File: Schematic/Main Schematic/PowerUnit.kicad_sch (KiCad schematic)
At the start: 19 parts

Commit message: Update
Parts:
- added TP13: TestPoint, symbol Connector:TestPoint
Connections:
- net at C?.1, J?.1 (Pin_1), J?.2 (Pin_2)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: now also TP13.1
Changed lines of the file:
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@@
   (junction (at 54.6608 57.2008) (diameter 0) (color 0 0 0 0)
+  )
+  (junction (at 56.4896 148.59) (diameter 0) (color 0 0 0 0)
   )
   (junction (at 142.24 45.72) (diameter 0) (color 0 0 0 0)
@@
     (stroke (width 0) (type default))
   )
-  (wire (pts (xy 53.086 148.59) (xy 63.5 148.59))
+  (wire (pts (xy 53.086 148.59) (xy 56.4896 148.59))
     (stroke (width 0) (type default))
   )
@@
   )
   (wire (pts (xy 99.06 77.47) (xy 99.06 88.9))
+    (stroke (width 0) (type default))
+  )
+  (wire (pts (xy 56.4896 148.59) (xy 63.5 148.59))
     (stroke (width 0) (type default))
   )
@@
   (hierarchical_label "3.3V" (shape input) (at 102.87 148.59 0) (fields_autoplaced)
     (effects (font (size 1.27 1.27)) (justify left))
-  )
-  (netclass_flag "" (length 3) (shape round) (at 57.15 148.59 0) (fields_autoplaced)
-    (effects (font (size 1.27 1.27)) (justify left bottom))
-    (property "Netclass" "" (at 57.8485 145.59 0)
-      (effects (font (size 1.27 1.27) italic) (justify left))
-    )
   )
   (symbol (lib_id "pspice:CAP") (at 53.086 156.21 0) (unit 1)
@@
         )
       )
+    )
+  )
+  (symbol (lib_id "Connector:TestPoint") (at 56.4896 148.59 0) (unit 1)
+    (in_bom yes) (on_board yes) (dnp no) (fields_autoplaced)
+    (property "Reference" "TP13" (at 58.42 144.653 0)
+      (effects (font (size 1.27 1.27)) (justify left))
+    )
+    (property "Value" "TestPoint" (at 58.42 147.193 0)
+      (effects (font (size 1.27 1.27)) (justify left))
+    )
+    (property "Footprint" "" (at 61.5696 148.59 0)
+      (effects (font (size 1.27 1.27)) hide)
+    )
+    (property "Datasheet" "~" (at 61.5696 148.59 0)
+      (effects (font (size 1.27 1.27)) hide)
+    )
+    (pin "1")
+    (instances
+      (project "Main Schematic"
+        (path "/81c41bad-bb43-41af-b405-18d135a809b1/297def35-fe1a-4185-9e34-6248c2c818f7"
+          (reference "TP13") (unit 1)
+        )
+      )

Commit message: assigned footprints for most of the components
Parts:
- C?: footprint (none) -> 10uFcapa:CAPC1608X100N
- R2: footprint (none) -> 1K_R:RESC1005X40N
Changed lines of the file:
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@@
       (effects (font (size 1.27 1.27)) (justify left))
     )
-    (property "Footprint" "" (at 110.1852 55.88 0)
+    (property "Footprint" "10uFcapa:CAPC1608X100N" (at 110.1852 55.88 0)
       (effects (font (size 1.27 1.27)) hide)
     )
@@
       (effects (font (size 1.27 1.27)) (justify left))
     )
-    (property "Footprint" "" (at 97.282 73.66 90)
+    (property "Footprint" "1K_R:RESC1005X40N" (at 97.282 73.66 90)
       (effects (font (size 1.27 1.27)) hide)
     )

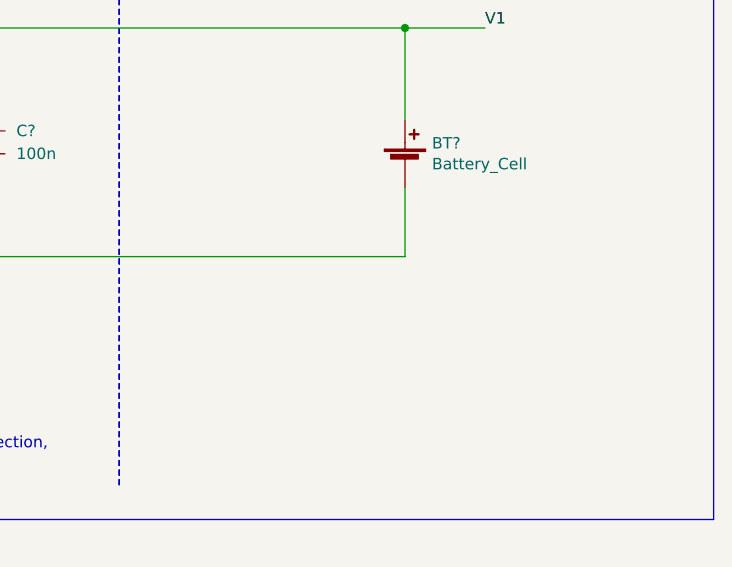
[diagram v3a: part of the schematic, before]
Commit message: Updated the footprints and the PCB
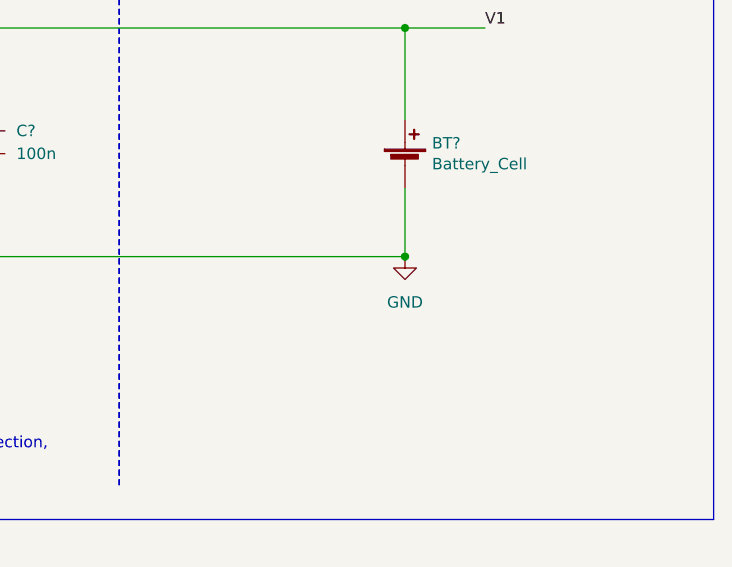
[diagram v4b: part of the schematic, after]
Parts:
- BT?: footprint (none) -> Battery:BatteryHolder_Keystone_3034_1x20mm
- C? (x3): footprint 10uFcapa:CAPC1608X100N -> Capacitor_SMD:C_0402_1005Metric
- C?: footprint (none) -> Capacitor_SMD:C_0201_0603Metric
- C?: footprint 10uFcapa:CAPC1608X100N -> Capacitor_SMD:C_1206_3216Metric_Pad1.33x1.80mm_HandSolder
- D1: footprint (none) -> Capacitor_SMD:C_1206_3216Metric
- J?: footprint (none) -> Connector_USB:USB_Micro-B_GCT_USB3076-30-A
- R3: footprint (none) -> Resistor_SMD:R_1206_3216Metric
- TP13: footprint (none) -> TestPoint:TestPoint_Pad_1.0x1.0mm
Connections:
- net GND: now also BT?.2 (-), C?.2, IC?.6 (GND), Q?.6 (S2_1), Q?.7 (S2_2)
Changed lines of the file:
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@@
   (junction (at 46.355 148.59) (diameter 0) (color 0 0 0 0)
+  )
+  (junction (at 251.46 83.82) (diameter 0) (color 0 0 0 0)
   )
   (junction (at 95.25 57.15) (diameter 0) (color 0 0 0 0)
@@
       (effects (font (size 1.27 1.27)) (justify left))
     )
-    (property "Footprint" "10uFcapa:CAPC1608X100N" (at 53.086 156.21 0)
+    (property "Footprint" "Capacitor_SMD:C_0402_1005Metric" (at 53.086 156.21 0)
       (effects (font (size 1.27 1.27)) hide)
     )
@@
       (effects (font (size 1.27 1.27)))
     )
-    (property "Footprint" "" (at 35.6108 74.93 0)
+    (property "Footprint" "Connector_USB:USB_Micro-B_GCT_USB3076-30-A" (at 35.6108 74.93 0)
       (effects (font (size 1.27 1.27)) hide)
     )
@@
       (effects (font (size 1.27 1.27)) (justify right))
     )
-    (property "Footprint" "" (at 99.06 92.71 0)
+    (property "Footprint" "Capacitor_SMD:C_1206_3216Metric" (at 99.06 92.71 0)
       (effects (font (size 1.27 1.27)) hide)
     )
@@
       (effects (font (size 1.27 1.27)) (justify left))
     )
-    (property "Footprint" "10uFcapa:CAPC1608X100N" (at 110.1852 55.88 0)
+    (property "Footprint" "Capacitor_SMD:C_0402_1005Metric" (at 110.1852 55.88 0)
       (effects (font (size 1.27 1.27)) hide)
     )
@@
       (effects (font (size 1.27 1.27)) (justify left))
     )
-    (property "Footprint" "" (at 96.2152 68.58 0)
+    (property "Footprint" "Capacitor_SMD:C_0201_0603Metric" (at 96.2152 68.58 0)
       (effects (font (size 1.27 1.27)) hide)
     )
@@
     )
   )
+  (symbol (lib_id "power:GND") (at 251.46 83.82 0) (unit 1)
+    (in_bom yes) (on_board yes) (dnp no) (fields_autoplaced)
+    (property "Reference" "#PWR?" (at 251.46 90.17 0)
+      (effects (font (size 1.27 1.27)) hide)
+    )
+    (property "Value" "GND" (at 251.46 88.9 0)
+      (effects (font (size 1.27 1.27)))
+    )
+    (property "Footprint" "" (at 251.46 83.82 0)
+      (effects (font (size 1.27 1.27)) hide)
+    )
+    (property "Datasheet" "" (at 251.46 83.82 0)
+      (effects (font (size 1.27 1.27)) hide)
+    )
+    (pin "1")
+    (instances
+      (project "power"
+        (path "/00318b70-98db-4150-aae9-0fe9db9b4f56"
+          (reference "#PWR?") (unit 1)
+        )
+      )
+      (project "Main Schematic"
+        (path "/81c41bad-bb43-41af-b405-18d135a809b1/297def35-fe1a-4185-9e34-6248c2c818f7"
+          (reference "#PWR03") (unit 1)
+        )
+      )
+    )
+  )
   (symbol (lib_id "pspice:CAP") (at 85.852 156.2608 0) (unit 1)
     (in_bom yes) (on_board yes) (dnp no) (fields_autoplaced)
@@
       (effects (font (size 1.27 1.27)) (justify left))
     )
-    (property "Footprint" "10uFcapa:CAPC1608X100N" (at 85.852 156.2608 0)
+    (property "Footprint" "Capacitor_SMD:C_0402_1005Metric" (at 85.852 156.2608 0)
       (effects (font (size 1.27 1.27)) hide)
     )
@@
       (effects (font (size 1.27 1.27)) (justify left))
     )
-    (property "Footprint" "10uFcapa:CAPC1608X100N" (at 203.2 71.12 0)
+    (property "Footprint" "Capacitor_SMD:C_1206_3216Metric_Pad1.33x1.80mm_HandSolder" (at 203.2 71.12 0)
       (effects (font (size 1.27 1.27)) hide)
     )
@@
       (effects (font (size 1.27 1.27)) (justify left))
     )
-    (property "Footprint" "" (at 251.46 72.136 90)
+    (property "Footprint" "Battery:BatteryHolder_Keystone_3034_1x20mm" (at 251.46 72.136 90)
       (effects (font (size 1.27 1.27)) hide)
     )
@@
       (effects (font (size 1.27 1.27)) (justify left))
     )
-    (property "Footprint" "" (at 61.5696 148.59 0)
+    (property "Footprint" "TestPoint:TestPoint_Pad_1.0x1.0mm" (at 61.5696 148.59 0)
       (effects (font (size 1.27 1.27)) hide)
     )
@@
       (effects (font (size 1.27 1.27)) (justify left))
     )
-    (property "Footprint" "" (at 104.902 74.93 90)
-      (effects (font (size 1.27 1.27)) hide)
-    )
+    (property "Footprint" "Resistor_SMD:R_1206_3216Metric" (at 104.902 74.93 90)
+      (effects (font (size 1.27 1.27)) hide)
+    )

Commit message: Updated
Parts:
- IC?: footprint DW:SOT95P280X135-6N -> SOT95P280X135-6N
- Q?: footprint FS82:SOP65P640X120-8N -> SOP65P640X120-8N; Manufacturer_Name fortune -> Fortune Semiconductor Corporation
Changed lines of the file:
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@@
   (symbol (lib_id "FS8205A:FS8205A") (at 152.4 78.74 0) (unit 1)
     (in_bom yes) (on_board yes) (dnp no) (fields_autoplaced)
-    (property "Reference" "Q?" (at 167.64 71.12 0)
-      (effects (font (size 1.27 1.27)))
-    )
-    (property "Value" "FS8205A" (at 167.64 73.66 0)
-      (effects (font (size 1.27 1.27)))
-    )
-    (property "Footprint" "FS82:SOP65P640X120-8N" (at 179.07 76.2 0)
-      (effects (font (size 1.27 1.27)) (justify left) hide)
-    )
-    (property "Datasheet" "http://www.ic-fortune.com/upload/Download/FS8205A-DS-12_EN.pdf" (at 179.07 78.74 0)
-      (effects (font (size 1.27 1.27)) (justify left) hide)
+    (property "Reference" "Q?" (at 167.64 72.39 0)
+      (effects (font (size 1.27 1.27)))
+    )
+    (property "Value" "FS8205A" (at 167.64 74.93 0)
+      (effects (font (size 1.27 1.27)))
+    )
+    (property "Footprint" "SOP65P640X120-8N" (at 179.07 173.66 0)
+      (effects (font (size 1.27 1.27)) (justify left top) hide)
+    )
+    (property "Datasheet" "http://www.ic-fortune.com/upload/Download/FS8205A-DS-12_EN.pdf" (at 179.07 273.66 0)
+      (effects (font (size 1.27 1.27)) (justify left top) hide)
     )
     (property "Description" "Dual N-Channel Enahncement Mode Power MOSFET" (at 179.07 81.28 0)
       (effects (font (size 1.27 1.27)) (justify left) hide)
     )
-    (property "Height" "1.2" (at 179.07 83.82 0)
-      (effects (font (size 1.27 1.27)) (justify left) hide)
-    )
-    (property "Manufacturer_Name" "fortune" (at 179.07 86.36 0)
-      (effects (font (size 1.27 1.27)) (justify left) hide)
-    )
-    (property "Manufacturer_Part_Number" "FS8205A" (at 179.07 88.9 0)
-      (effects (font (size 1.27 1.27)) (justify left) hide)
-    )
-    (property "Mouser Part Number" "" (at 179.07 91.44 0)
-      (effects (font (size 1.27 1.27)) (justify left) hide)
-    )
-    (property "Mouser Price/Stock" "" (at 179.07 93.98 0)
-      (effects (font (size 1.27 1.27)) (justify left) hide)
-    )
-    (property "Arrow Part Number" "" (at 179.07 96.52 0)
-      (effects (font (size 1.27 1.27)) (justify left) hide)
-    )
-    (property "Arrow Price/Stock" "" (at 179.07 99.06 0)
-      (effects (font (size 1.27 1.27)) (justify left) hide)
+    (property "Height" "1.2" (at 179.07 473.66 0)
+      (effects (font (size 1.27 1.27)) (justify left top) hide)
+    )
+    (property "Manufacturer_Name" "Fortune Semiconductor Corporation" (at 179.07 573.66 0)
+      (effects (font (size 1.27 1.27)) (justify left top) hide)
+    )
+    (property "Manufacturer_Part_Number" "FS8205A" (at 179.07 673.66 0)
+      (effects (font (size 1.27 1.27)) (justify left top) hide)
+    )
+    (property "Mouser Part Number" "" (at 179.07 773.66 0)
+      (effects (font (size 1.27 1.27)) (justify left top) hide)
+    )
+    (property "Mouser Price/Stock" "" (at 179.07 873.66 0)
+      (effects (font (size 1.27 1.27)) (justify left top) hide)
+    )
+    (property "Arrow Part Number" "" (at 179.07 973.66 0)
+      (effects (font (size 1.27 1.27)) (justify left top) hide)
+    )
+    (property "Arrow Price/Stock" "" (at 179.07 1073.66 0)
+      (effects (font (size 1.27 1.27)) (justify left top) hide)
     )
     (pin "1")
@@
   (symbol (lib_id "DW01A-G:DW01A-G") (at 152.4 55.88 0) (unit 1)
     (in_bom yes) (on_board yes) (dnp no) (fields_autoplaced)
-    (property "Reference" "IC?" (at 165.1 48.26 0)
-      (effects (font (size 1.27 1.27)))
-    )
-    (property "Value" "DW01A-G" (at 165.1 50.8 0)
-      (effects (font (size 1.27 1.27)))
-    )
-    (property "Footprint" "DW:SOT95P280X135-6N" (at 173.99 53.34 0)
-      (effects (font (size 1.27 1.27)) (justify left) hide)
-    )
-    (property "Datasheet" "http://acoptex.com/uploads/DW01A.pdf" (at 173.99 55.88 0)
-      (effects (font (size 1.27 1.27)) (justify left) hide)
+    (property "Reference" "IC?" (at 165.1 49.53 0)
+      (effects (font (size 1.27 1.27)))
+    )
+    (property "Value" "DW01A-G" (at 165.1 52.07 0)
+      (effects (font (size 1.27 1.27)))
+    )
+    (property "Footprint" "SOT95P280X135-6N" (at 173.99 150.8 0)
+      (effects (font (size 1.27 1.27)) (justify left top) hide)
+    )
+    (property "Datasheet" "http://acoptex.com/uploads/DW01A.pdf" (at 173.99 250.8 0)
+      (effects (font (size 1.27 1.27)) (justify left top) hide)
     )
     (property "Description" "One Cell Lithium-ion/Polymer Battery Protection IC" (at 173.99 58.42 0)
       (effects (font (size 1.27 1.27)) (justify left) hide)
     )
-    (property "Height" "1.35" (at 173.99 60.96 0)
-      (effects (font (size 1.27 1.27)) (justify left) hide)
-    )
-    (property "Manufacturer_Name" "Fortune Semiconductor Corporation" (at 173.99 63.5 0)
-      (effects (font (size 1.27 1.27)) (justify left) hide)
-    )
-    (property "Manufacturer_Part_Number" "DW01A-G" (at 173.99 66.04 0)
-      (effects (font (size 1.27 1.27)) (justify left) hide)
-    )
-    (property "Mouser Part Number" "" (at 173.99 68.58 0)
-      (effects (font (size 1.27 1.27)) (justify left) hide)
-    )
-    (property "Mouser Price/Stock" "" (at 173.99 71.12 0)
-      (effects (font (size 1.27 1.27)) (justify left) hide)
-    )
-    (property "Arrow Part Number" "" (at 173.99 73.66 0)
-      (effects (font (size 1.27 1.27)) (justify left) hide)
-    )
-    (property "Arrow Price/Stock" "" (at 173.99 76.2 0)
-      (effects (font (size 1.27 1.27)) (justify left) hide)
-    )
-    (pin "1")
+    (property "Height" "1.35" (at 173.99 450.8 0)
+      (effects (font (size 1.27 1.27)) (justify left top) hide)
+    )
+    (property "Manufacturer_Name" "Fortune Semiconductor Corporation" (at 173.99 550.8 0)
+      (effects (font (size 1.27 1.27)) (justify left top) hide)
+    )
+    (property "Manufacturer_Part_Number" "DW01A-G" (at 173.99 650.8 0)
+      (effects (font (size 1.27 1.27)) (justify left top) hide)
+    )
+    (property "Mouser Part Number" "" (at 173.99 750.8 0)
+      (effects (font (size 1.27 1.27)) (justify left top) hide)
+    )
+    (property "Mouser Price/Stock" "" (at 173.99 850.8 0)
+      (effects (font (size 1.27 1.27)) (justify left top) hide)
+    )
+    (property "Arrow Part Number" "" (at 173.99 950.8 0)
+      (effects (font (size 1.27 1.27)) (justify left top) hide)
+    )
+    (property "Arrow Price/Stock" "" (at 173.99 1050.8 0)
+      (effects (font (size 1.27 1.27)) (justify left top) hide)
+    )
+    (pin "1")

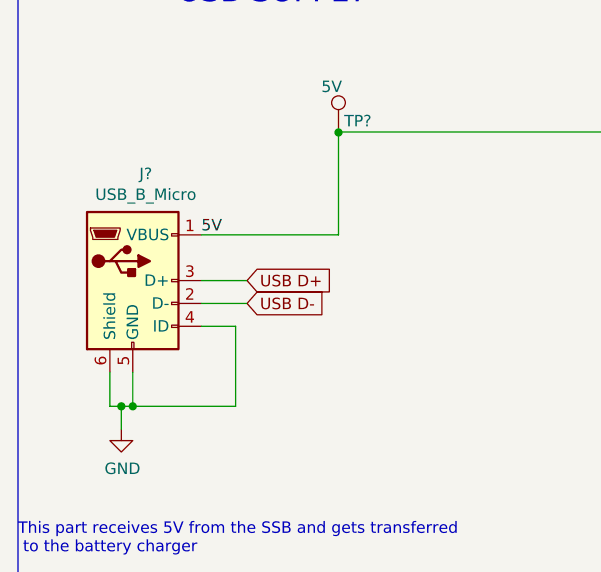
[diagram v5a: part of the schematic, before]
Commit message: I Fixed the connections on the power module ,because the jumper was not cinnected properly
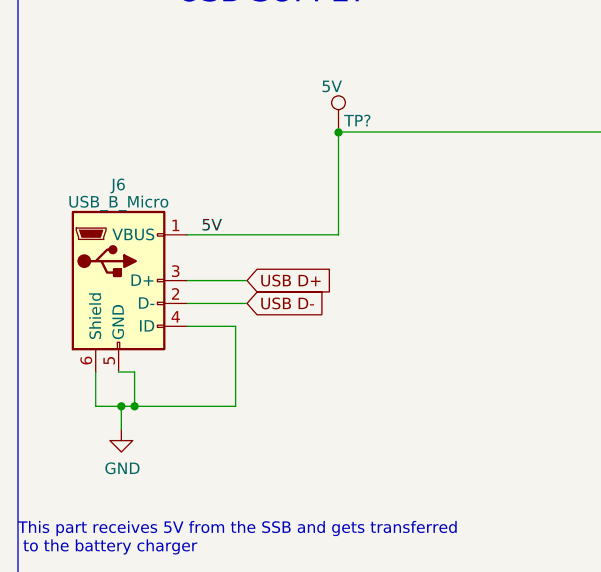
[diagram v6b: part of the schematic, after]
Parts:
- removed J?: USB_B_Micro, Connector_USB:USB_Micro-B_GCT_USB3076-30-A, symbol Connector:USB_B_Micro
- added J6: USB_B_Micro, symbol Connector:USB_B_Micro
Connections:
- net 5V: now also J6.1 (VBUS)
- net GND: now also J6.4 (ID), J6.5 (GND), J6.6 (Shield)
- net USB D+: now also J6.3 (D+)
- net USB D-: now also J6.2 (D-)
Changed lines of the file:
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@@
   (junction (at 195.58 83.82) (diameter 0) (color 0 0 0 0)
   )
+  (junction (at 32.004 87.63) (diameter 0) (color 0 0 0 0)
+  )
   (junction (at 104.14 57.15) (diameter 0) (color 0 0 0 0)
-  )
-  (junction (at 31.8008 87.63) (diameter 0) (color 0 0 0 0)
   )
   (junction (at 203.2 58.42) (diameter 0) (color 0 0 0 0)
@@
     (stroke (width 0) (type default))
   )
+  (wire (pts (xy 32.004 87.63) (xy 43.2308 87.63))
+    (stroke (width 0) (type default))
+  )
   (wire (pts (xy 85.852 148.59) (xy 85.852 149.9108))
     (stroke (width 0) (type default))
@@
     (stroke (width 0) (type default))
   )
-  (wire (pts (xy 30.5308 87.63) (xy 31.8008 87.63))
-    (stroke (width 0) (type default))
-  )
   (wire (pts (xy 53.086 148.59) (xy 53.086 149.86))
     (stroke (width 0) (type default))
@@
     (stroke (width 0) (type default))
   )
-  (wire (pts (xy 39.4208 76.2) (xy 44.5008 76.2))
+  (wire (pts (xy 37.846 76.2) (xy 44.5008 76.2))
     (stroke (width 0) (type default))
   )
@@
     (stroke (width 0) (type default))
   )
-  (wire (pts (xy 31.8008 87.63) (xy 31.8008 83.82))
-    (stroke (width 0) (type default))
-  )
   (wire (pts (xy 135.89 68.58) (xy 135.89 99.06))
     (stroke (width 0) (type default))
@@
     (stroke (width 0) (type default))
   )
-  (wire (pts (xy 30.5308 87.63) (xy 29.2608 87.63))
+  (wire (pts (xy 27.686 87.63) (xy 30.5308 87.63))
     (stroke (width 0) (type default))
   )
@@
     (stroke (width 0) (type default))
   )
-  (wire (pts (xy 39.4208 78.74) (xy 43.2308 78.74))
+  (wire (pts (xy 37.846 78.74) (xy 43.2308 78.74))
     (stroke (width 0) (type default))
   )
@@
     (stroke (width 0) (type default))
   )
+  (wire (pts (xy 27.686 87.63) (xy 27.686 83.82))
+    (stroke (width 0) (type default))
+  )
   (wire (pts (xy 251.46 58.42) (xy 260.35 58.42))
     (stroke (width 0) (type default))
@@
     (stroke (width 0) (type default))
   )
+  (wire (pts (xy 32.004 83.82) (xy 32.004 87.63))
+    (stroke (width 0) (type default))
+  )
   (wire (pts (xy 109.22 45.72) (xy 109.22 48.26))
     (stroke (width 0) (type default))
@@
     (stroke (width 0) (type default))
   )
-  (wire (pts (xy 43.2308 87.63) (xy 31.8008 87.63))
+  (wire (pts (xy 30.5308 87.63) (xy 32.004 87.63))
     (stroke (width 0) (type default))
   )
@@
     (stroke (width 0) (type default))
   )
-  (wire (pts (xy 29.2608 87.63) (xy 29.2608 83.82))
-    (stroke (width 0) (type default))
-  )
   (wire (pts (xy 147.32 60.96) (xy 152.4 60.96))
     (stroke (width 0) (type default))
@@
     (stroke (width 0) (type default))
   )
-  (wire (pts (xy 39.4208 68.58) (xy 54.6608 68.58))
+  (wire (pts (xy 37.846 68.58) (xy 54.6608 68.58))
+    (stroke (width 0) (type default))
+  )
+  (wire (pts (xy 30.226 83.82) (xy 32.004 83.82))
     (stroke (width 0) (type default))
   )
@@
     (stroke (width 0) (type default))
   )
-  (wire (pts (xy 39.4208 73.66) (xy 44.5008 73.66))
+  (wire (pts (xy 37.846 73.66) (xy 44.5008 73.66))
     (stroke (width 0) (type default))
   )
@@
         (path "/81c41bad-bb43-41af-b405-18d135a809b1/297def35-fe1a-4185-9e34-6248c2c818f7"
           (reference "#PWR010") (unit 1)
-        )
-      )
-    )
-  )
-  (symbol (lib_id "Connector:USB_B_Micro") (at 31.8008 73.66 0) (unit 1)
-    (in_bom yes) (on_board yes) (dnp no)
-    (property "Reference" "J?" (at 33.2486 61.7982 0)
-      (effects (font (size 1.27 1.27)))
-    )
-    (property "Value" "USB_B_Micro" (at 33.2486 64.1096 0)
-      (effects (font (size 1.27 1.27)))
-    )
-    (property "Footprint" "Connector_USB:USB_Micro-B_GCT_USB3076-30-A" (at 35.6108 74.93 0)
-      (effects (font (size 1.27 1.27)) hide)
-    )
-    (property "Datasheet" "~" (at 35.6108 74.93 0)
-      (effects (font (size 1.27 1.27)) hide)
-    )
-    (pin "1")
-    (pin "2")
-    (pin "3")
-    (pin "4")
-    (pin "5")
-    (pin "6")
-    (instances
-      (project "Main Schematic"
-        (path "/7e8c9ffe-1b32-4326-ae61-8877b5395b8a/98e117a5-3aeb-416f-98c5-160b7cf15fec"
-          (reference "J?") (unit 1)
-        )
-      )
-      (project "Main Schematic"
-        (path "/81c41bad-bb43-41af-b405-18d135a809b1"
-          (reference "J?") (unit 1)
-        )
-        (path "/81c41bad-bb43-41af-b405-18d135a809b1/297def35-fe1a-4185-9e34-6248c2c818f7"
-          (reference "J6") (unit 1)
-        )
-      )
-      (project "PowerUnit_sch"
-        (path "/94a75581-cd2d-4b84-bb57-dd404d2f6711"
-          (reference "J?") (unit 1)
-        )
-      )
-      (project "power supplly[2803]"
-        (path "/ef6f5e70-2168-4df2-b1ca-c7d9a0d51980"
-          (reference "J?") (unit 1)
         )
       )
@@
         )
       )
+    )
+  )
+  (symbol (lib_id "Connector:USB_B_Micro") (at 30.226 73.66 0) (unit 1)
+    (in_bom yes) (on_board yes) (dnp no) (fields_autoplaced)
+    (property "Reference" "J6" (at 30.226 63.0301 0)
+      (effects (font (size 1.27 1.27)))
+    )
+    (property "Value" "USB_B_Micro" (at 30.226 64.9511 0)
+      (effects (font (size 1.27 1.27)))
+    )
+    (property "Footprint" "" (at 34.036 74.93 0)
+      (effects (font (size 1.27 1.27)) hide)
+    )
+    (property "Datasheet" "~" (at 34.036 74.93 0)
+      (effects (font (size 1.27 1.27)) hide)
+    )
+    (pin "1")
+    (pin "2")
+    (pin "3")
+    (pin "4")
+    (pin "5")
+    (pin "6")
+    (instances
+      (project "Main Schematic"
+        (path "/81c41bad-bb43-41af-b405-18d135a809b1/297def35-fe1a-4185-9e34-6248c2c818f7"
+          (reference "J6") (unit 1)
+        )
+      )
